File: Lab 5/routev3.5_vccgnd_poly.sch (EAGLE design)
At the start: 48 parts, among them J1 FTDI_DEVICERA_SMT, M1 WIRELESS-NRF24L01, U2 GY-521MPU6050, U3 ATMEGA328P_TQFP

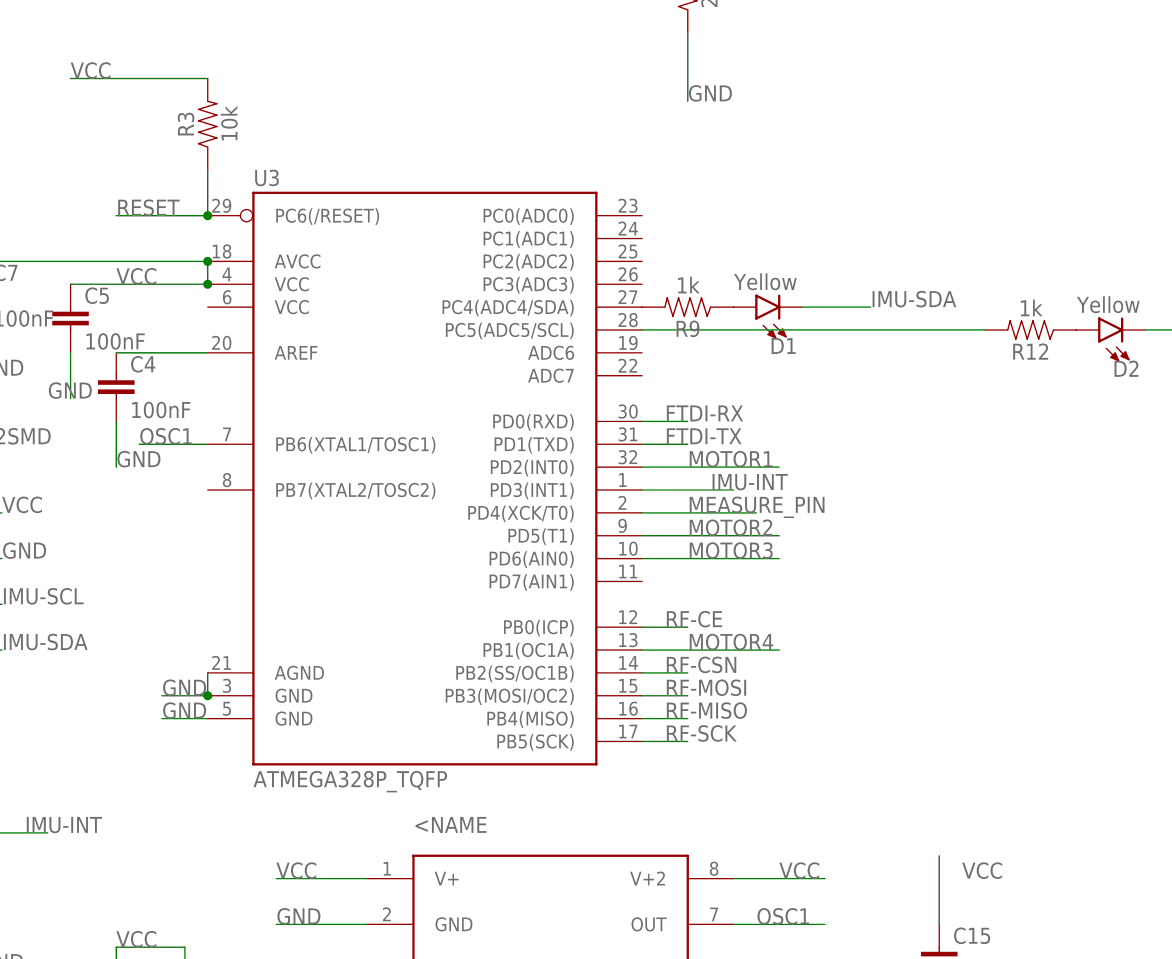
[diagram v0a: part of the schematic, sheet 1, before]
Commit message: Update template file, switch for the right Atmega MCU. Some advice from Arti:   - Everything need to be inside the board (all white frames inside): quadcopter propellers need clearance.   - Nothing under white frame except the Radio Module   - Battery JBT need to have +- on the edge of the PCB   - Mandatory: Top Polygon: VCC, Bottom Polygon: GND; Don't worry about Digital and Analog VCC and GND.
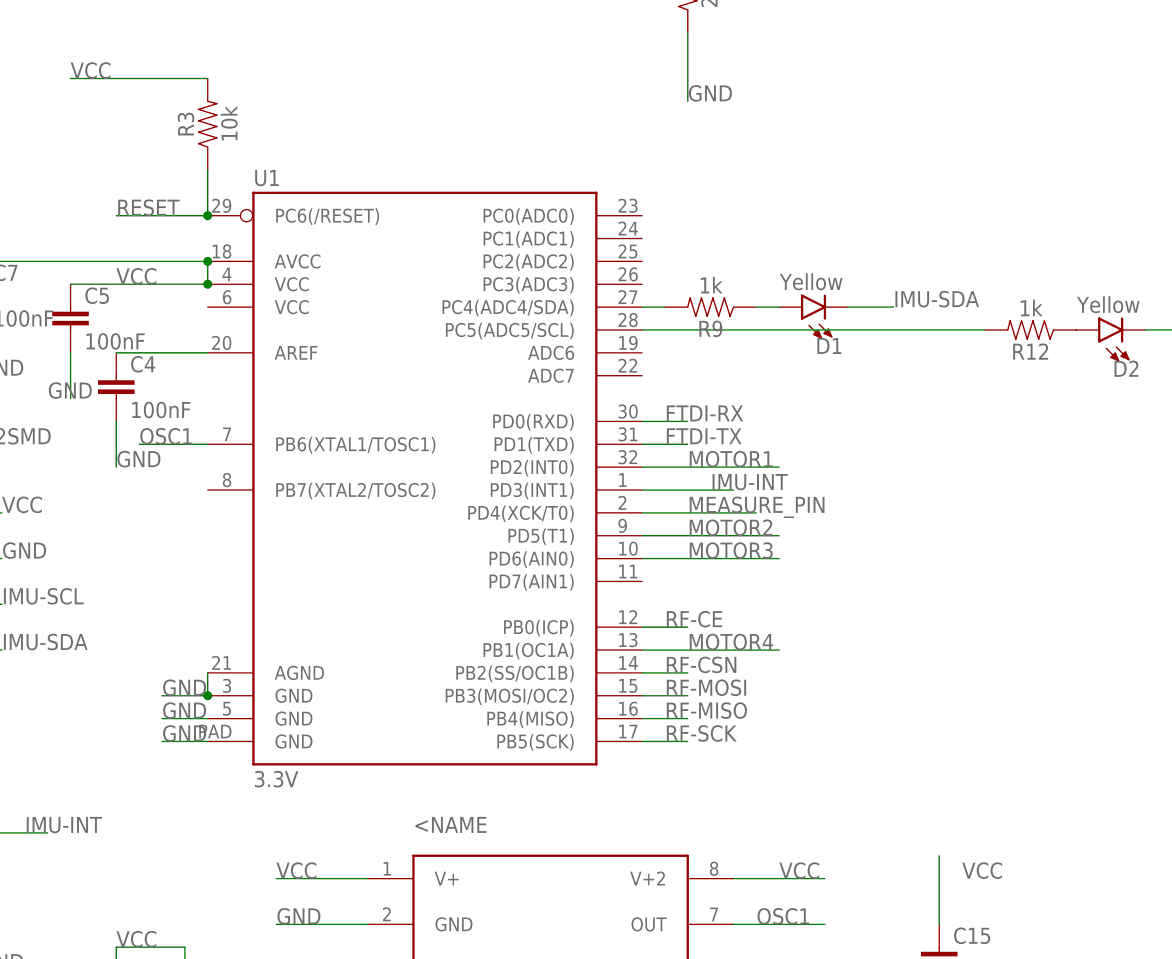
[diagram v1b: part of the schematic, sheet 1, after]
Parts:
- removed U3: ATMEGA328P_TQFP, quad:ATMEGA328P_TQFP
- added U1: 3.3V, SparkFun-DigitalIC:ATMEGA328P_MLFMLF32
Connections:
- removed net N$8 (its old number): R9.2, U3.PC4(ADC4/SDA)
- new net N$3: R9.2, U1.PC4(ADC4/SDA)
- net FTDI-RX: now also U1.PD0(RXD); no longer U3.PD0(RXD)
- net FTDI-TX: now also U1.PD1(TXD); no longer U3.PD1(TXD)
- net GND: now also U1.AGND, U1.GND@3, U1.GND@5, U1.GND@PAD; no longer U3.AGND, U3.GND@3, U3.GND@5
- net IMU-INT: now also U1.PD3(INT1); no longer U3.PD3(INT1)
- net MEASURE_PIN: now also U1.PD4(XCK/T0); no longer U3.PD4(XCK/T0)
- net MOTOR1: now also U1.PD2(INT0); no longer U3.PD2(INT0)
- net MOTOR2: now also U1.PD5(T1); no longer U3.PD5(T1)
- net MOTOR3: now also U1.PD6(AIN0); no longer U3.PD6(AIN0)
- net MOTOR4: now also U1.PB1(OC1A); no longer U3.PB1(OC1A)
- net N$10: now also U1.PC5(ADC5/SCL); no longer U3.PC5(ADC5/SCL)
- net N$2: now also U1.AREF; no longer U3.AREF
- net OSC1: now also U1.PB6(XTAL1/TOSC1); no longer U3.PB6(XTAL1/TOSC1)
- net RESET: now also U1.PC6(/RESET); no longer U3.PC6(/RESET)
- net RF-CE: now also U1.PB0(ICP); no longer U3.PB0(ICP)
- net RF-CSN: now also U1.PB2(SS/OC1B); no longer U3.PB2(SS/OC1B)
- net RF-MISO: now also U1.PB4(MISO); no longer U3.PB4(MISO)
- net RF-MOSI: now also U1.PB3(MOSI/OC2); no longer U3.PB3(MOSI/OC2)
- net RF-SCK: now also U1.PB5(SCK); no longer U3.PB5(SCK)
- net VCC: now also U1.AVCC, U1.VCC@4; no longer U3.AVCC, U3.VCC@4
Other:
- moved on the sheet: D1, R9
